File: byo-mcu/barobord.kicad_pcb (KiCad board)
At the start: 2 copper layers, 243.2 x 136.2 mm, 132 parts, among them J1 Pimoroni, SW1 SW_Push, SW10 SW_Push, SW11 SW_Push, SW12 SW_Push, SW13 SW_Push, SW14 SW_Push, SW15 SW_Push, SW16 SW_Push, SW17 SW_Push, SW18 SW_Push, SW19 SW_Push, SW2 SW_Push, SW20 SW_Push, SW21 SW_Push, SW22 SW_Push, SW23 SW_Push, SW24 SW_Push, SW25 SW_Push, SW26 SW_Push, SW27 SW_Push, SW28 SW_Push, SW29 SW_Push, SW3 SW_Push, SW30 SW_Push, SW31 SW_Push, SW32 SW_Push, SW33 SW_Push, SW34 SW_Push, SW35 SW_Push, SW36 SW_Push, SW37 SW_Push, SW38 SW_Push, SW39 SW_Push, SW4 SW_Push, SW40 SW_Push, SW41 SW_Push, SW42 RotaryEncoder_Switch, SW43 RotaryEncoder_Switch, SW44 EVQWGD001, SW45 EVQWGD001, SW5 SW_Push, SW6 SW_Push, SW7 SW_Push, SW8 SW_Push, SW9 SW_Push, U1 Elite-C, U2 nice_nano

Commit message: updated byo-mcu to work
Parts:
- added J2: Conn_01x02_Female, Connector_JST:JST_PH_S2B-PH-K_1x02_P2.00mm_Horizontal, B.Cu at (91.5, 102.1)
- added SW46: SW_DIP_x01, Button_Switch_THT:SW_CuK_OS102011MA1QN1_SPDT_Angled, B.Cu at (124.3, 152.9)
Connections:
- D10 pad 1: row0 -> row4
- D20 pad 1: row1 -> row4
- D30 pad 1: row2 -> row4
- D40 pad 1: row3 -> row4
- D81 pad 1: row2 -> row4
- D82 pad 1: row3 -> row4
- SW10 pad 2: col9 -> col5
- SW20 pad 2: col9 -> col6
- SW30 pad 2: col9 -> col7
- SW40 pad 2: col9 -> col8
- SW42 pad S1: col10 -> col4
- SW43 pad S1: col10 -> col3
- SW44 pad S1: col10 -> col4
- SW45 pad S1: col10 -> col3
- U1 pad 13: ENC2A -> row0
- U1 pad 14: col10 -> row4
- U1 pad 15: col9 -> ENC2A
- U1 pad 23: GND -> B-
- U1 pad 24: row0 -> B+
- U2 pad 13: ENC2A -> row0
- U2 pad 14: col10 -> row4
- U2 pad 15: col9 -> ENC2A
- U2 pad 23: GND -> B-
- U2 pad 24: row0 -> B+
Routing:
- net row4: track 0.00 -> 265.6 mm, vias 0 -> 12
- net col9: track 208.0 -> 0.00 mm, vias 7 -> 0
- net B+: track 0.00 -> 149.6 mm, vias 0 -> 5
- net col10: track 134.8 -> 0.00 mm, vias 6 -> 0
- net B-: track 0.00 -> 127.2 mm, vias 0 -> 5
- net col5: track 122.8 -> 217.7 mm, vias 3 -> 5
- net Net-(J2-Pad1): track 0.00 -> 77.1 mm, vias 0 -> 4
- net col6: track 143.9 -> 215.4 mm, vias 3 -> 5
- net col3: track 148.8 -> 214.4 mm, vias 4 -> 8
- net col7: track 209.3 -> 267.7 mm, vias 6 -> 10
- net row2: track 390.8 -> 333.4 mm, vias 17 -> 13
- net row1: track 386.1 -> 351.1 mm, vias 15 -> 14
- net row3: track 464.4 -> 439.3 mm, vias 16 -> 14
- net col4: track 115.4 -> 137.5 mm, vias 2 -> 3
- net col8: track 190.5 -> 204.1 mm
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
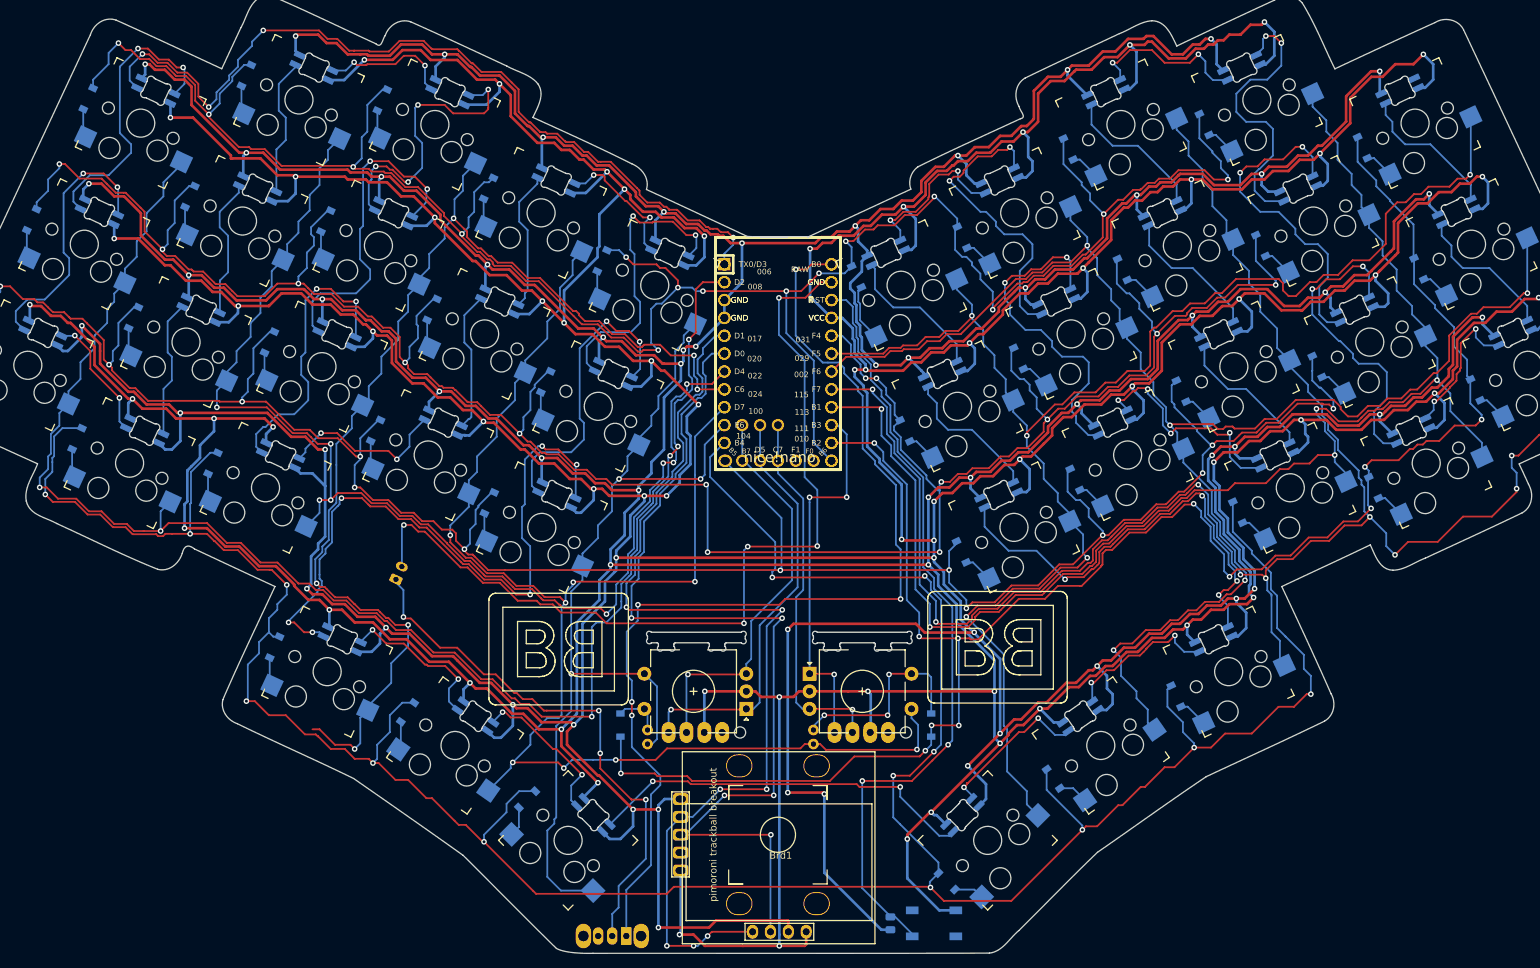
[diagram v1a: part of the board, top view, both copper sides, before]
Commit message: added mounting holes for byo-mcu, and moved the on off switch to the top of the board
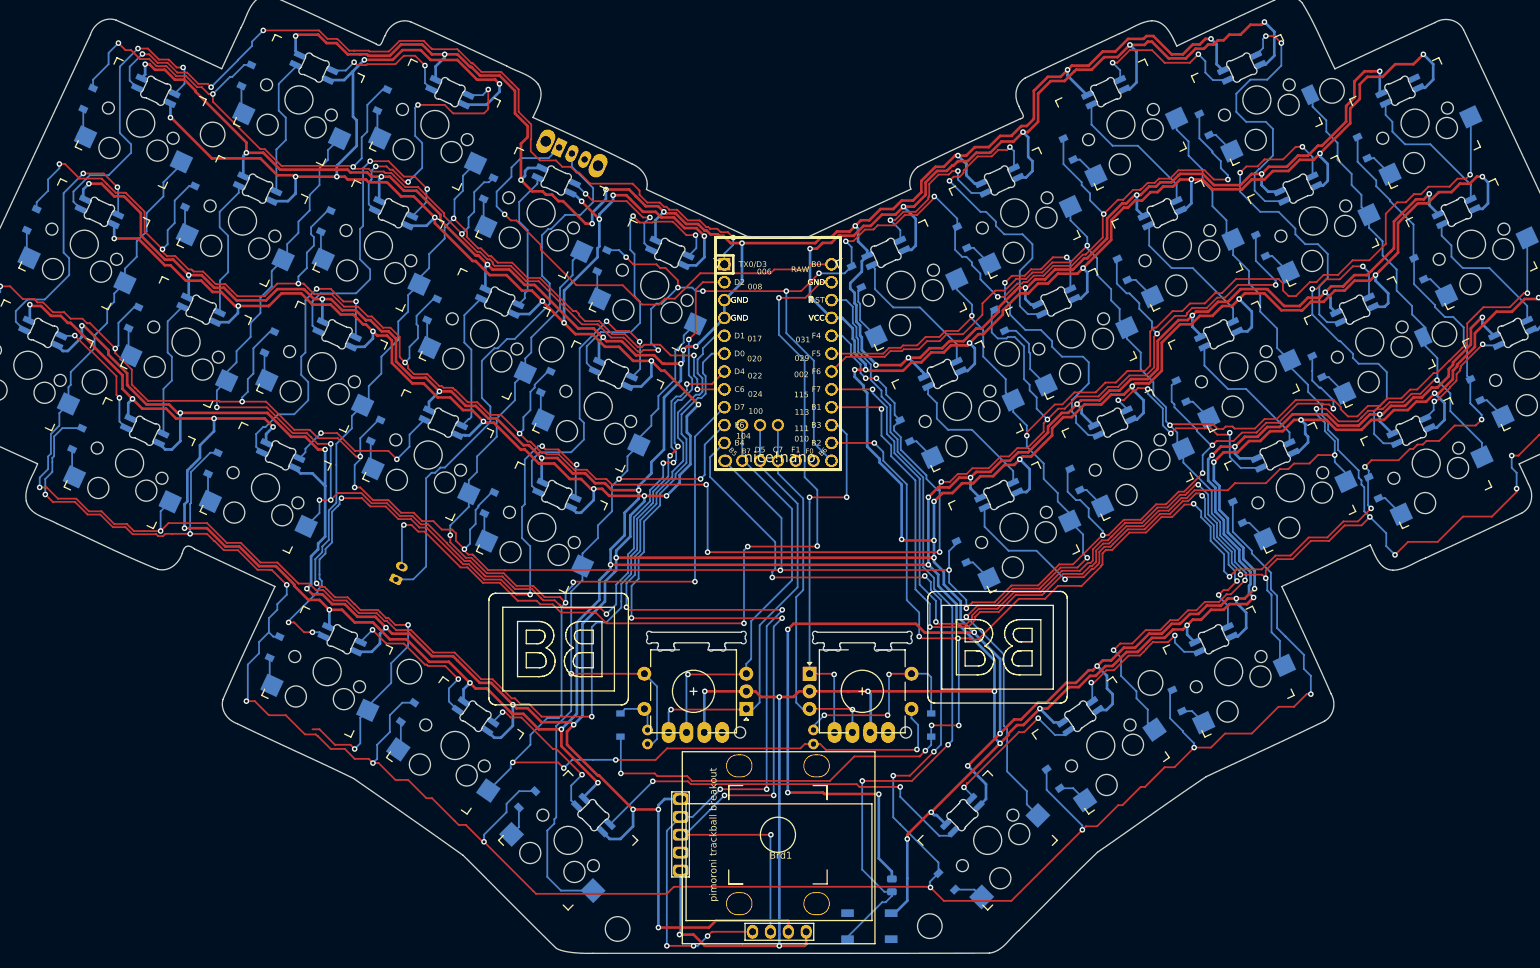
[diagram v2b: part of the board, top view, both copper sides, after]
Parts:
- added ?: , MountingHole:MountingHole_3.5mm, F.Cu at (198.9, 116.9)
- added ?: , MountingHole:MountingHole_3.5mm, F.Cu at (65.5, 38.9)
- added ?: , MountingHole:MountingHole_3.5mm, F.Cu at (240.7, 67.3)
- added ?: , MountingHole:MountingHole_3.5mm, F.Cu at (224.7, 32.7)
- added ?: , MountingHole:MountingHole_3.5mm, F.Cu at (178.4, 70.1)
- added ?: , MountingHole:MountingHole_3.5mm, F.Cu at (167.5, 151.5)
- added ?: , MountingHole:MountingHole_3.5mm, F.Cu at (123.1, 151.9)
- added ?: , MountingHole:MountingHole_3.5mm, F.Cu at (93.4, 115.3)
- added ?: , MountingHole:MountingHole_3.5mm, F.Cu at (113.7, 69.5)
- added ?: , MountingHole:MountingHole_3.5mm, F.Cu at (48.7, 74.1)
- moved SW46 112.5 mm to (114.7, 40.7), turned to 335 degrees
- moved SW41 9.20 mm to (158.9, 151.5)
- moved D17 6.06 mm to (177.4, 65.3)
- moved R4 5.40 mm to (162.1, 145.7), turned to 270 degrees
- moved D38 0.66 mm to (202.6, 119.4)
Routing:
- net B+: track 149.6 -> 70.9 mm, vias 5 -> 1
- net +5V: track 1388.1 -> 1372.8 mm, vias 64 -> 66
- net row1: track 351.1 -> 359.0 mm
- net GND: track 1286.4 -> 1293.6 mm, vias 62 -> 64
- net row0: track 324.0 -> 317.1 mm
- net Net-(D17-Pad2): track 4.17 -> 11.1 mm
- net Net-(D77-Pad2): track 20.8 -> 16.4 mm
- net row2: track 333.4 -> 330.5 mm
- net Net-(J2-Pad1): track 77.1 -> 79.9 mm, vias 4 -> 0
- net led: track 120.7 -> 118.1 mm
- net RESET: track 112.3 -> 113.9 mm
- net Net-(D54-Pad2): track 19.3 -> 18.0 mm
- net row3: track 439.3 -> 438.4 mm
- net row4: track 265.6 -> 266.3 mm
- net col6: track 215.4 -> 215.9 mm
